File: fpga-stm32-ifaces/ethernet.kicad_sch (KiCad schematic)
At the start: 75 parts, among them J1 0826-1G1T-23-F, J2 PMOD_HOST, U10 ECS-1612MV-250-CN, U2 XC7S25-1FTGB196, U3 ECS-1612MV-250-CN, U4 KSZ9031RN, U5 RCLAMP0514M, U6 RCLAMP0514M, U7 ECS-1612MV-250-CN

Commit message: Finished initial schematic of fpga-stm32-ifaces board, waiting for sch review
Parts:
- removed U3: ECS-1612MV-250-CN, azonenberg_pcb:OSCILLATOR_1.6x1.2, symbol osc-azonenberg:OSC
- added C57, C58: 0.47 uF, azonenberg_pcb:EIA_0402_CAP_NOSILK, symbol device:C
- added R80: 1K, azonenberg_pcb:EIA_0402_RES_NOSILK, symbol device:R
- added R81, R82, R83, R84: 33, azonenberg_pcb:EIA_0402_RES_NOSILK, symbol device:R
- added U3: S25FL128SAGBHIA10, azonenberg_pcb:BGA_24_6x8_DEPOP1_1MM, symbol memory-azonenberg:S25FLxxxS_BGA24_5x5_VIO
- C1: value 0.47 uF -> 4.7 uF; footprint azonenberg_pcb:EIA_0402_CAP_NOSILK -> azonenberg_pcb:EIA_0603_CAP_NOSILK
- R35: value 33 -> 4.7K
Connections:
- net 3V3: now also R35.2, C57.1, C58.1, R80.1, U3.B4 (VDD), U3.E4 (VIO)
- net ETH_CLK_25MHZ: no longer R35.1
- net FPGA_FLASH_CS_N: now also R35.1, U3.C2 (CS_N)
- net FPGA_FLASH_DQ0: now also R81.2
- net FPGA_FLASH_DQ1: now also R82.2
- net FPGA_FLASH_DQ2: now also R83.2
- net FPGA_FLASH_DQ3: now also R84.2
- net FPGA_FLASH_SCK: now also U3.B2 (SCK)
- net GND: now also C57.2, C58.2, U3.B3 (VSS)
- new net: R80.2, U3.A4 (RESET_N)
- new net: R81.1, U3.D3 (MOSI/DQ0)
- new net: R82.1, U3.D2 (MISO/DQ1)
- new net: R83.1, U3.C4 (WP_N/DQ2)
- new net: R84.1, U3.D4 (RESET_N/DQ3)
- no-connect marks 3 -> 24
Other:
- moved on the sheet: C33, R57, U10

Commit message: Continued initial layout of fpga-stm32-ifaces
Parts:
- J2: footprint (none) -> azonenberg_pcb:CONN_HEADER_2.54MM_2x6_RA_PMOD_HOST
- U2: footprint (none) -> azonenberg_pcb:BGA_196_15x15_FULLARRAY_1MM_FTGB196
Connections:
- net ETH_RXD0: now also U2.C12 (IO_L6N_T0_D08_VREF_14); no longer U2.L14 (IO_L15N_T2_DQS_DOUT_CSO_B_14)
- net ETH_RXD1: now also U2.D12 (IO_L8P_T1_D11_14); no longer U2.L12 (IO_L16P_T2_CSI_B_14)
- net ETH_RXD2: now also U2.C14 (IO_L11N_T1_SRCC_14); no longer U2.L13 (IO_L16N_T2_D31_14)
- net ETH_RXD3: now also U2.D13 (IO_L8N_T1_D12_14); no longer U2.J11 (IO_L17P_T2_D30_14)
- net RGMII_TXD0: now also U2.A13 (IO_L4N_T0_D05_14); no longer U2.F14 (IO_L9N_T1_DQS_D13_14)
- net RGMII_TXD1: now also U2.A12 (IO_L4P_T0_D04_14); no longer U2.G14 (IO_L9P_T1_DQS_14)
- net RGMII_TXD2: now also U2.A10 (IO_L3N_T0_DQS_EMCCLK_14); no longer U2.D13 (IO_L8N_T1_D12_14)
- net RGMII_TXD3: now also U2.B13 (IO_L5P_T0_D06_14); no longer U2.D12 (IO_L8P_T1_D11_14)
- net RGMII_TX_CLK: now also U2.B14 (IO_L5N_T0_D07_14); no longer U2.E12 (IO_L7N_T1_D10_14)
- net RGMII_TX_EN: now also U2.D14 (IO_L11P_T1_SRCC_14); no longer U2.J12 (IO_L17N_T2_D29_14)
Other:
- company: (none) -> Antikernel Labs
- title: (none) -> FPGA - STM32 Interface Test
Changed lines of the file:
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@@
 	(generator_version "8.0")
 	(paper "A3")
+	(title_block
+		(title "FPGA - STM32 Interface Test")
+		(date "2024-06-12")
+		(rev "0.1")
+		(company "Antikernel Labs")
+	)
 	(junction
 		(at 100.33 50.8)
@@
 	)
 	(no_connect
-		(at 354.33 59.69)
-	)
-	(no_connect
 		(at 354.33 82.55)
 	)
 	(no_connect
-		(at 354.33 64.77)
+		(at 354.33 115.57)
 	)
 	(no_connect
-		(at 354.33 90.17)
+		(at 354.33 69.85)
 	)
 	(no_connect
-		(at 354.33 54.61)
+		(at 354.33 110.49)
 	)
 	(no_connect
-		(at 354.33 130.81)
+		(at 354.33 80.01)
 	)
 	(no_connect
-		(at 354.33 57.15)
+		(at 354.33 113.03)
 	)
 	(no_connect
-		(at 354.33 95.25)
+		(at 354.33 130.81)
 	)
 	(no_connect
-		(at 354.33 87.63)
+		(at 354.33 95.25)
 	)
 	(no_connect
@@
 	)
 	(no_connect
-		(at 354.33 49.53)
+		(at 354.33 118.11)
+	)
+	(no_connect
+		(at 354.33 120.65)
 	)
 	(no_connect
@@
 	)
 	(no_connect
+		(at 354.33 77.47)
+	)
+	(no_connect
 		(at 157.48 104.14)
 	)
@@
 	)
 	(no_connect
-		(at 354.33 52.07)
-	)
-	(no_connect
 		(at 354.33 85.09)
 	)
@@
 	)
 	(label "RGMII_TX_CLK"
-		(at 354.33 69.85 180)
+		(at 354.33 59.69 180)
 		(fields_autoplaced yes)
 		(effects
@@
 	)
 	(label "RGMII_TXD1"
-		(at 354.33 77.47 180)
+		(at 354.33 52.07 180)
 		(fields_autoplaced yes)
 		(effects
@@
 	)
 	(label "RGMII_TX_EN"
-		(at 354.33 120.65 180)
+		(at 354.33 87.63 180)
 		(fields_autoplaced yes)
 		(effects
@@
 	)
 	(label "RGMII_TXD0"
-		(at 354.33 80.01 180)
+		(at 354.33 54.61 180)
 		(fields_autoplaced yes)
 		(effects
@@
 	)
 	(label "ETH_RXD2"
-		(at 354.33 115.57 180)
+		(at 354.33 90.17 180)
 		(fields_autoplaced yes)
 		(effects
@@
 	)
 	(label "RGMII_TXD2"
-		(at 354.33 74.93 180)
+		(at 354.33 49.53 180)
 		(fields_autoplaced yes)
 		(effects
@@
 	)
 	(label "RGMII_TXD3"
-		(at 354.33 72.39 180)
+		(at 354.33 57.15 180)
 		(fields_autoplaced yes)
 		(effects
@@
 	)
 	(label "ETH_RXD0"
-		(at 354.33 110.49 180)
+		(at 354.33 64.77 180)
 		(fields_autoplaced yes)
 		(effects
@@
 	)
 	(label "ETH_RXD3"
-		(at 354.33 118.11 180)
+		(at 354.33 74.93 180)
 		(fields_autoplaced yes)
 		(effects
@@
 	)
 	(label "ETH_RXD1"
-		(at 354.33 113.03 180)
+		(at 354.33 72.39 180)
 		(fields_autoplaced yes)
 		(effects
@@
 			)
 		)
-		(property "Footprint" ""
+		(property "Footprint" "azonenberg_pcb:BGA_196_15x15_FULLARRAY_1MM_FTGB196"
 			(at 359.41 160.02 0)
 			(effects
@@
 			)
 		)
-		(property "Footprint" ""
+		(property "Footprint" "azonenberg_pcb:CONN_HEADER_2.54MM_2x6_RA_PMOD_HOST"
 			(at 359.41 209.55 0)
 			(effects

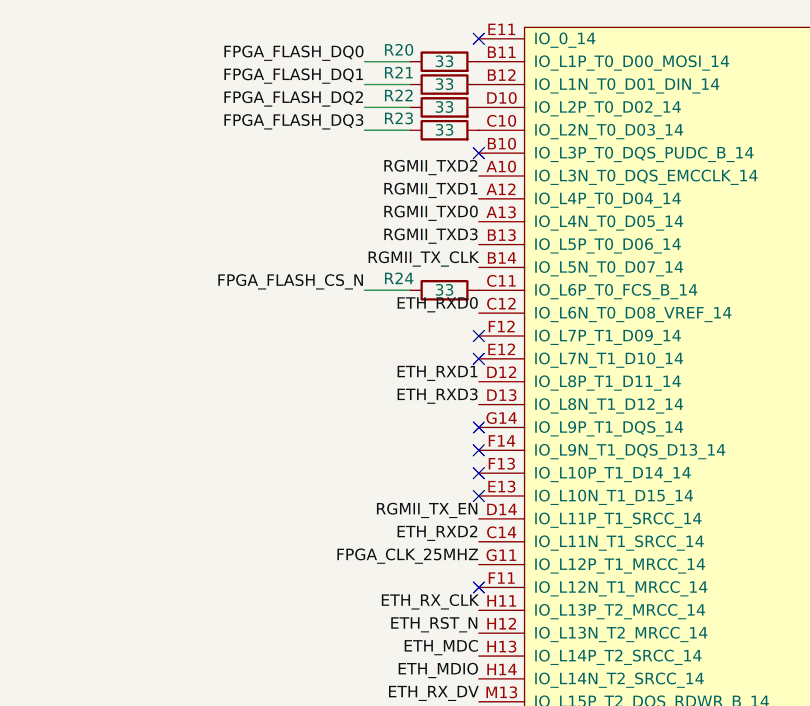
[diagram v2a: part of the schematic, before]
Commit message: Routed most FPGA decoupling caps plus most of RGMII
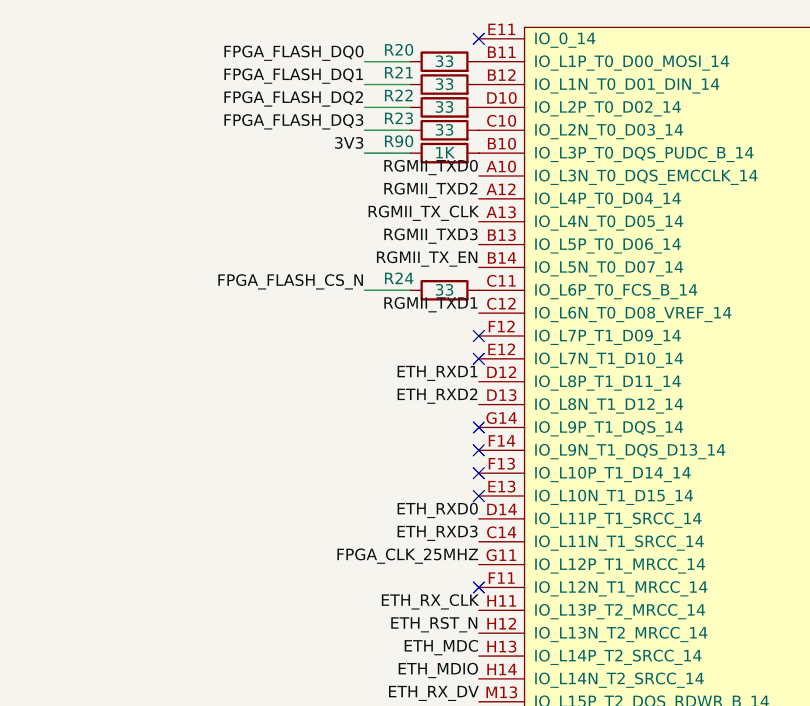
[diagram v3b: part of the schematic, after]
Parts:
- added R90: 1K, azonenberg_pcb:EIA_0402_RES_NOSILK, symbol device:R
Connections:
- net 3V3: now also R90.1
- net ETH_RXD0: now also U2.D14 (IO_L11P_T1_SRCC_14); no longer U2.C12 (IO_L6N_T0_D08_VREF_14)
- net ETH_RXD2: now also U2.D13 (IO_L8N_T1_D12_14); no longer U2.C14 (IO_L11N_T1_SRCC_14)
- net ETH_RXD3: now also U2.C14 (IO_L11N_T1_SRCC_14); no longer U2.D13 (IO_L8N_T1_D12_14)
- net RGMII_TXD0: now also U2.A10 (IO_L3N_T0_DQS_EMCCLK_14); no longer U2.A13 (IO_L4N_T0_D05_14)
- net RGMII_TXD1: now also U2.C12 (IO_L6N_T0_D08_VREF_14); no longer U2.A12 (IO_L4P_T0_D04_14)
- net RGMII_TXD2: now also U2.A12 (IO_L4P_T0_D04_14); no longer U2.A10 (IO_L3N_T0_DQS_EMCCLK_14)
- net RGMII_TX_CLK: now also U2.A13 (IO_L4N_T0_D05_14); no longer U2.B14 (IO_L5N_T0_D07_14)
- net RGMII_TX_EN: now also U2.B14 (IO_L5N_T0_D07_14); no longer U2.D14 (IO_L11P_T1_SRCC_14)
- net at U2.B10 (IO_L3P_T0_DQS_PUDC_B_14): now also R90.2
- no-connect marks 24 -> 23
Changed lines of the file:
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@@
 	)
 	(no_connect
-		(at 354.33 46.99)
-	)
-	(no_connect
 		(at 354.33 133.35)
 	)
@@
 	(wire
 		(pts
+			(xy 341.63 46.99) (xy 346.71 46.99)
+		)
+		(stroke
+			(width 0)
+			(type default)
+		)
+	)
+	(wire
+		(pts
 			(xy 341.63 44.45) (xy 346.71 44.45)
 		)
@@
 	)
 	(label "RGMII_TX_CLK"
-		(at 354.33 59.69 180)
+		(at 354.33 54.61 180)
 		(fields_autoplaced yes)
 		(effects
@@
 	)
 	(label "RGMII_TXD1"
-		(at 354.33 52.07 180)
+		(at 354.33 64.77 180)
 		(fields_autoplaced yes)
 		(effects
@@
 	)
 	(label "RGMII_TX_EN"
-		(at 354.33 87.63 180)
+		(at 354.33 59.69 180)
 		(fields_autoplaced yes)
 		(effects
@@
 	)
 	(label "RGMII_TXD0"
-		(at 354.33 54.61 180)
+		(at 354.33 49.53 180)
 		(fields_autoplaced yes)
 		(effects
@@
 	)
 	(label "ETH_RXD2"
-		(at 354.33 90.17 180)
+		(at 354.33 74.93 180)
 		(fields_autoplaced yes)
 		(effects
@@
 	)
 	(label "RGMII_TXD2"
-		(at 354.33 49.53 180)
+		(at 354.33 52.07 180)
 		(fields_autoplaced yes)
 		(effects
@@
 		)
 	)
+	(label "3V3"
+		(at 341.63 46.99 180)
+		(fields_autoplaced yes)
+		(effects
+			(font
+				(size 1.27 1.27)
+			)
+			(justify right bottom)
+		)
+	)
 	(label "FPGA_PMOD_DQ0"
 		(at 354.33 190.5 180)
@@
 	)
 	(label "ETH_RXD0"
-		(at 354.33 64.77 180)
+		(at 354.33 87.63 180)
 		(fields_autoplaced yes)
 		(effects
@@
 	)
 	(label "ETH_RXD3"
-		(at 354.33 74.93 180)
+		(at 354.33 90.17 180)
 		(fields_autoplaced yes)
 		(effects
@@
 					(unit 1)
 				)
+			)
+		)
+	)
+	(symbol
+		(lib_id "device:R")
+		(at 350.52 46.99 90)
+		(unit 1)
+		(exclude_from_sim no)
+		(in_bom yes)
+		(on_board yes)
+		(dnp no)
+		(property "Reference" "R90"
+			(at 345.44 45.72 90)
+			(effects
+				(font
+					(size 1.27 1.27)
+				)
+			)
+		)
+		(property "Value" "1K"
+			(at 350.52 46.99 90)
+			(effects
+				(font
+					(size 1.27 1.27)
+				)
+			)
+		)
+		(property "Footprint" "azonenberg_pcb:EIA_0402_RES_NOSILK"
+			(at 350.52 48.768 90)
+			(effects
+				(font
+					(size 1.27 1.27)
+				)
+				(hide yes)
+			)
+		)
+		(property "Datasheet" ""
+			(at 350.52 46.99 0)
+			(effects
+				(font
+					(size 1.27 1.27)
+				)
+				(hide yes)
+			)
+		)
+		(property "Description" ""
+			(at 350.52 46.99 0)
+			(effects
+				(font
+					(size 1.27 1.27)
+				)
+				(hide yes)
+			)
+		)
+		(pin "1"
+		)
+		(pin "2"
+		)
+		(instances
+			(project "fpga-stm32-ifaces"
+				(path "/b35a72f3-8995-417e-af27-dca34b6125a3/a004f346-e36c-499d-9c4d-a7c3dff3eae4"
+					(reference "R90")
+					(unit 1)
+				)

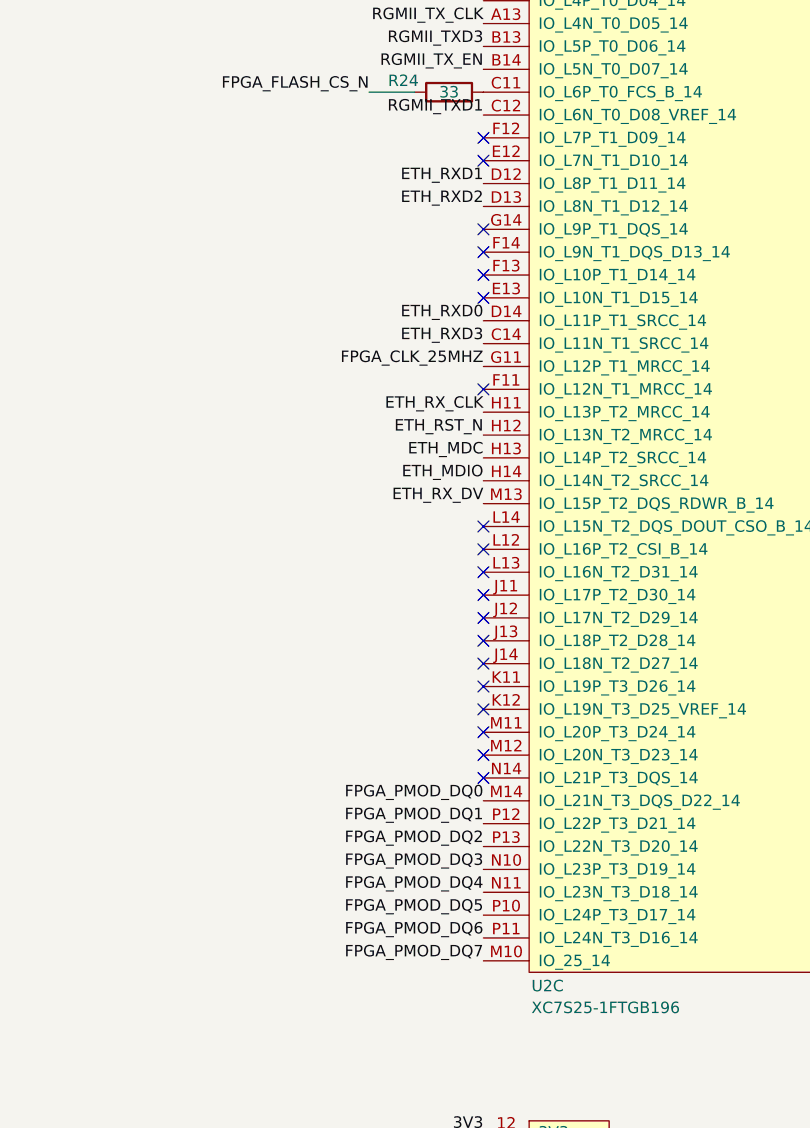
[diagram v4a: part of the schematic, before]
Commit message: Lots more routing around FPGA and MCU
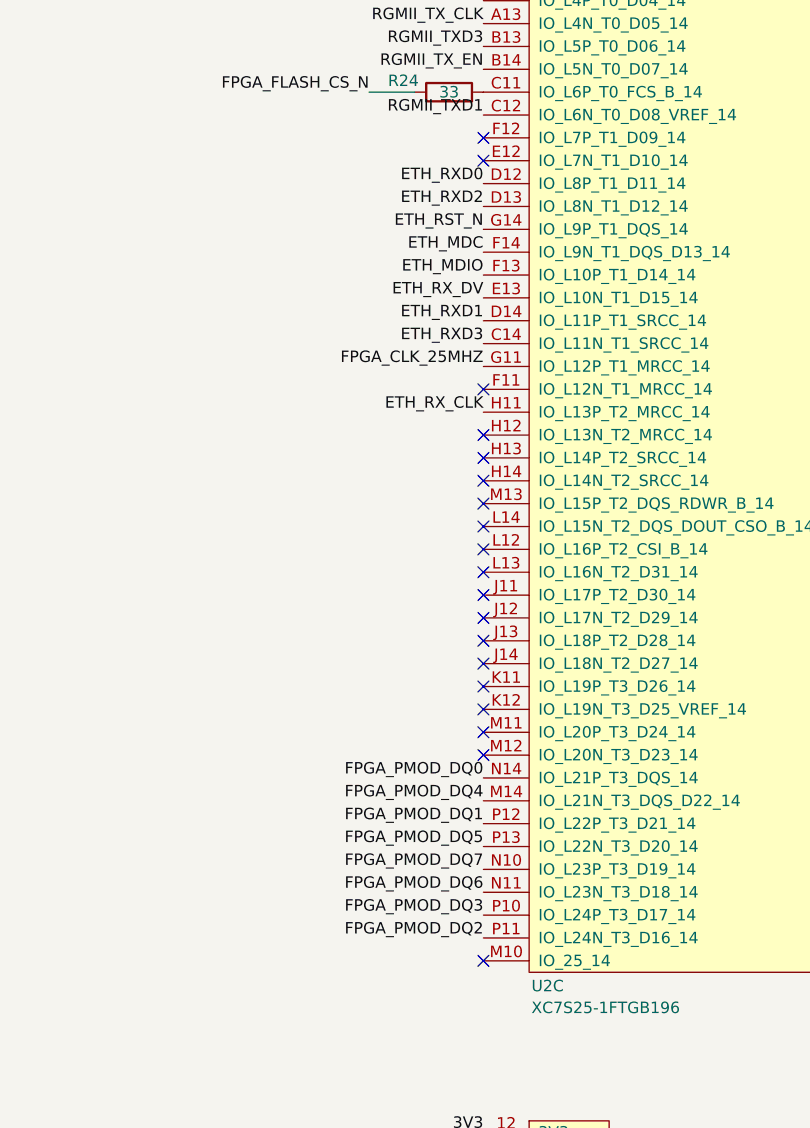
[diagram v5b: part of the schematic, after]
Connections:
- net ETH_MDC: now also U2.F14 (IO_L9N_T1_DQS_D13_14); no longer U2.H13 (IO_L14P_T2_SRCC_14)
- net ETH_MDIO: now also U2.F13 (IO_L10P_T1_D14_14); no longer U2.H14 (IO_L14N_T2_SRCC_14)
- net ETH_RST_N: now also U2.G14 (IO_L9P_T1_DQS_14); no longer U2.H12 (IO_L13N_T2_MRCC_14)
- net ETH_RXD0: now also U2.D12 (IO_L8P_T1_D11_14); no longer U2.D14 (IO_L11P_T1_SRCC_14)
- net ETH_RXD1: now also U2.D14 (IO_L11P_T1_SRCC_14); no longer U2.D12 (IO_L8P_T1_D11_14)
- net ETH_RX_DV: now also U2.E13 (IO_L10N_T1_D15_14); no longer U2.M13 (IO_L15P_T2_DQS_RDWR_B_14)
- net FPGA_PMOD_DQ0: now also U2.N14 (IO_L21P_T3_DQS_14); no longer U2.M14 (IO_L21N_T3_DQS_D22_14)
- net FPGA_PMOD_DQ2: now also U2.P11 (IO_L24N_T3_D16_14); no longer U2.P13 (IO_L22N_T3_D20_14)
- net FPGA_PMOD_DQ3: now also U2.P10 (IO_L24P_T3_D17_14); no longer U2.N10 (IO_L23P_T3_D19_14)
- net FPGA_PMOD_DQ4: now also U2.M14 (IO_L21N_T3_DQS_D22_14); no longer U2.N11 (IO_L23N_T3_D18_14)
- net FPGA_PMOD_DQ5: now also U2.P13 (IO_L22N_T3_D20_14); no longer U2.P10 (IO_L24P_T3_D17_14)
- net FPGA_PMOD_DQ6: now also U2.N11 (IO_L23N_T3_D18_14); no longer U2.P11 (IO_L24N_T3_D16_14)
- net FPGA_PMOD_DQ7: now also U2.N10 (IO_L23P_T3_D19_14); no longer U2.M10 (IO_25_14)
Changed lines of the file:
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@@
-	)
-	(no_connect
-		(at 354.33 82.55)
 	)
 	(no_connect
@@
 	)
 	(no_connect
+		(at 354.33 107.95)
+	)
+	(no_connect
 		(at 354.33 110.49)
 	)
 	(no_connect
-		(at 354.33 80.01)
+		(at 354.33 100.33)
 	)
 	(no_connect
@@
 	)
 	(no_connect
+		(at 354.33 105.41)
+	)
+	(no_connect
 		(at 354.33 130.81)
+	)
+	(no_connect
+		(at 354.33 158.75)
 	)
 	(no_connect
@@
 	)
 	(no_connect
-		(at 354.33 138.43)
-	)
-	(no_connect
 		(at 100.33 85.09)
 	)
@@
 	)
 	(no_connect
-		(at 354.33 77.47)
+		(at 157.48 104.14)
 	)
 	(no_connect
-		(at 157.48 104.14)
+		(at 354.33 102.87)
 	)
 	(no_connect
 		(at 354.33 133.35)
-	)
-	(no_connect
-		(at 354.33 85.09)
 	)
 	(no_connect
@@
 	)
 	(label "ETH_MDC"
-		(at 354.33 102.87 180)
+		(at 354.33 80.01 180)
 		(fields_autoplaced yes)
 		(effects
@@
 	)
 	(label "ETH_MDIO"
-		(at 354.33 105.41 180)
+		(at 354.33 82.55 180)
 		(fields_autoplaced yes)
 		(effects
@@
 	)
 	(label "ETH_RST_N"
-		(at 354.33 100.33 180)
+		(at 354.33 77.47 180)
 		(fields_autoplaced yes)
 		(effects
@@
 	)
 	(label "ETH_RX_DV"
-		(at 354.33 107.95 180)
+		(at 354.33 85.09 180)
 		(fields_autoplaced yes)
 		(effects
@@
 	)
 	(label "FPGA_PMOD_DQ4"
-		(at 354.33 151.13 180)
+		(at 354.33 140.97 180)
 		(fields_autoplaced yes)
 		(effects
@@
 	)
 	(label "FPGA_PMOD_DQ6"
-		(at 354.33 156.21 180)
+		(at 354.33 151.13 180)
 		(fields_autoplaced yes)
 		(effects
@@
 	)
 	(label "FPGA_PMOD_DQ0"
-		(at 354.33 140.97 180)
+		(at 354.33 138.43 180)
 		(fields_autoplaced yes)
 		(effects
@@
 	)
 	(label "FPGA_PMOD_DQ7"
-		(at 354.33 158.75 180)
+		(at 354.33 148.59 180)
 		(fields_autoplaced yes)
 		(effects
@@
 	)
 	(label "FPGA_PMOD_DQ2"
-		(at 354.33 146.05 180)
+		(at 354.33 156.21 180)
 		(fields_autoplaced yes)
 		(effects
@@
 	)
 	(label "ETH_RXD0"
-		(at 354.33 87.63 180)
+		(at 354.33 72.39 180)
 		(fields_autoplaced yes)
 		(effects
@@
 	)
 	(label "FPGA_PMOD_DQ3"
-		(at 354.33 148.59 180)
+		(at 354.33 153.67 180)
 		(fields_autoplaced yes)
 		(effects
@@
 	)
 	(label "ETH_RXD1"
-		(at 354.33 72.39 180)
+		(at 354.33 87.63 180)
 		(fields_autoplaced yes)
 		(effects
@@
 	)
 	(label "FPGA_PMOD_DQ5"
-		(at 354.33 153.67 180)
-		(fields_autoplaced yes)
-		(effects
+		(at 354.33 146.05 180)
+		(fields_autoplaced yes)
+		(effects
